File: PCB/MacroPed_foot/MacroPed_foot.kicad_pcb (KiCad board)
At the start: 2 copper layers, 24 x 51 mm, 6 parts, among them J9 Conn_01x02_Socket, SW1 SW_SPST

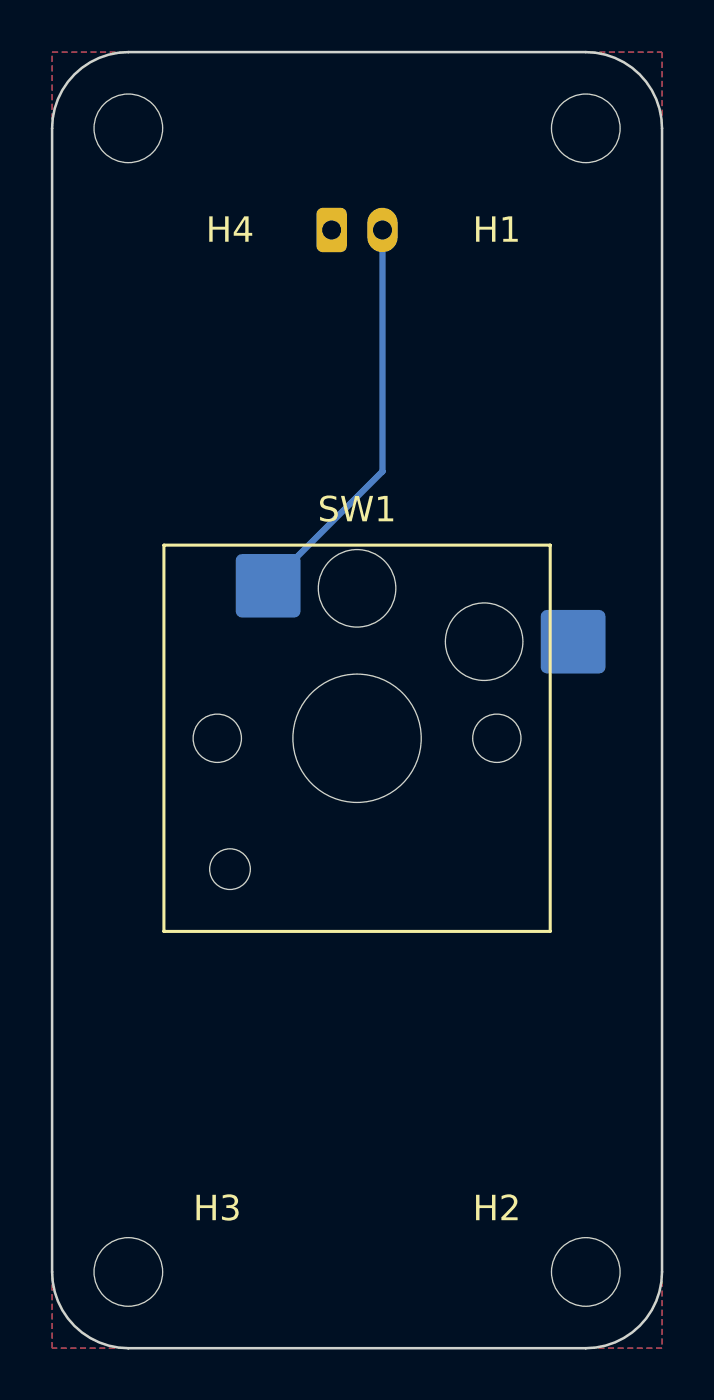
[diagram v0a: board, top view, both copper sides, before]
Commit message: Moved JST connector to edge of footboard
Signed-off-by: Devnol <pgkoutsoumanis@gmail.com>
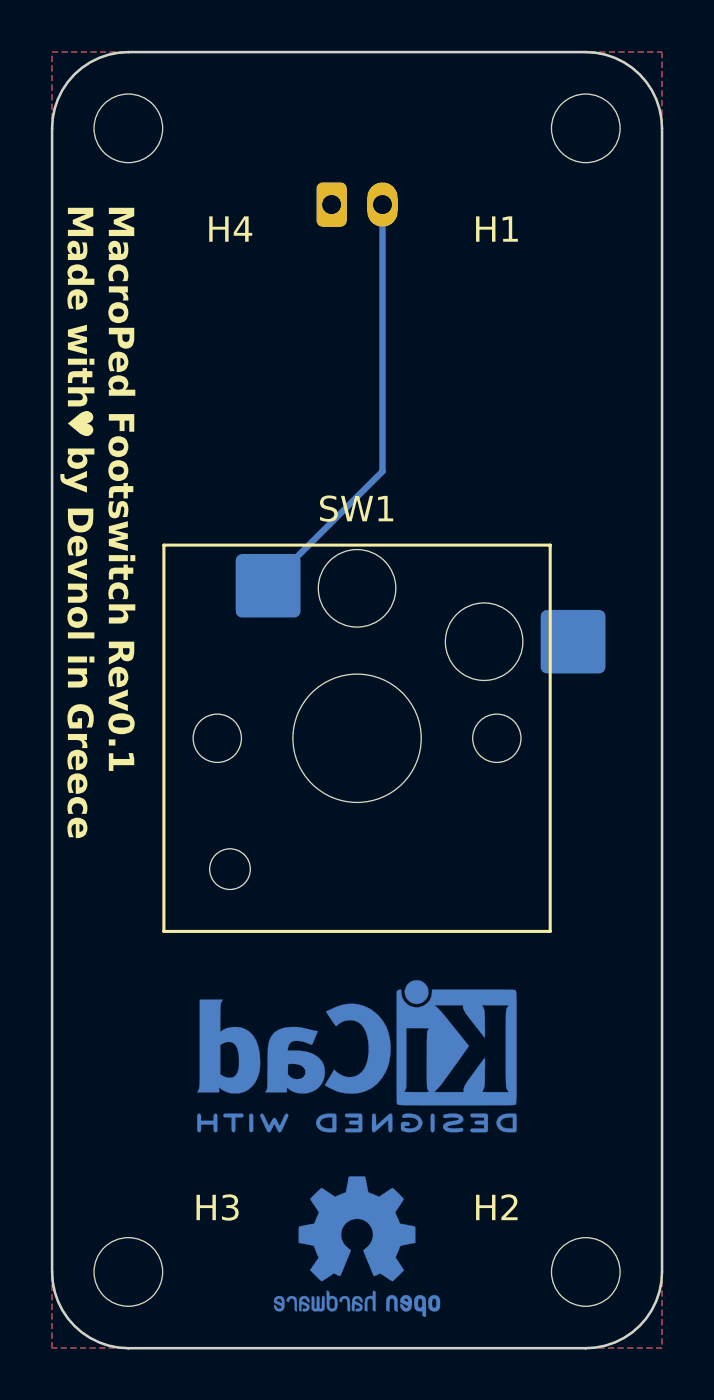
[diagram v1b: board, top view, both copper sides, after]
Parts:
- added REF**: KiCad-Logo2_5mm_Copper, Symbol:KiCad-Logo2_5mm_Copper, B.Cu at (105.0, 61.5)
- added REF**: OSHW-Logo2_7.3x6mm_Copper, Symbol:OSHW-Logo2_7.3x6mm_Copper, B.Cu at (105.0, 69.0)
- moved J1 1.00 mm to (104.0, 28.0)
- renumbered J9 to J1
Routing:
- net Net-(J9-Pin_2): track 15.9 -> 16.9 mm
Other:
- board text added: "MacroPed Footswitch Rev0.1 Made with by Devnol in Greece"
- board text added: "♥︎"

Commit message: Shorten main board
Signed-off-by: Devnol <pgkoutsoumanis@gmail.com>
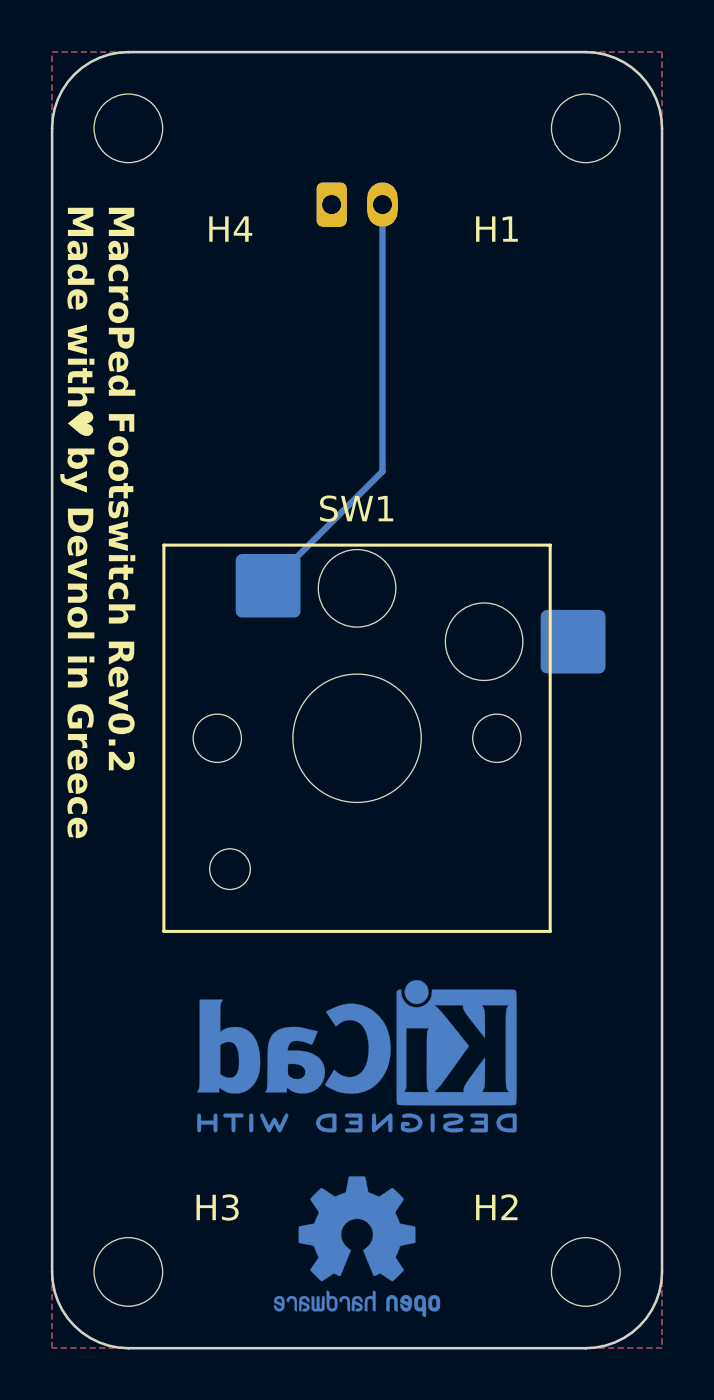
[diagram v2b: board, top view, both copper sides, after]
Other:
- board text added: "MacroPed Footswitch Rev0.2 Made with by Devnol in Greece"
- board text removed: "MacroPed Footswitch Rev0.1 Made with by Devnol in Greece"
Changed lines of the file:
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@@
   (gr_line (start 114 73) (end 96 73)
     (stroke (width 0.1) (type default)) (layer "Edge.Cuts"))
-  (gr_text "MacroPed Footswitch Rev0.1\nMade with   by Devnol in Greece" (at 93.5 28 270) (layer "F.SilkS")
+  (gr_text "MacroPed Footswitch Rev0.2\nMade with   by Devnol in Greece" (at 93.5 28 270) (layer "F.SilkS")
     (effects (font (size 1 1) (thickness 0.25) bold) (justify left bottom))
   )
